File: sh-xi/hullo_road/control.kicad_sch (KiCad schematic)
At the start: 1 part, among them U1 ATtiny414-SS

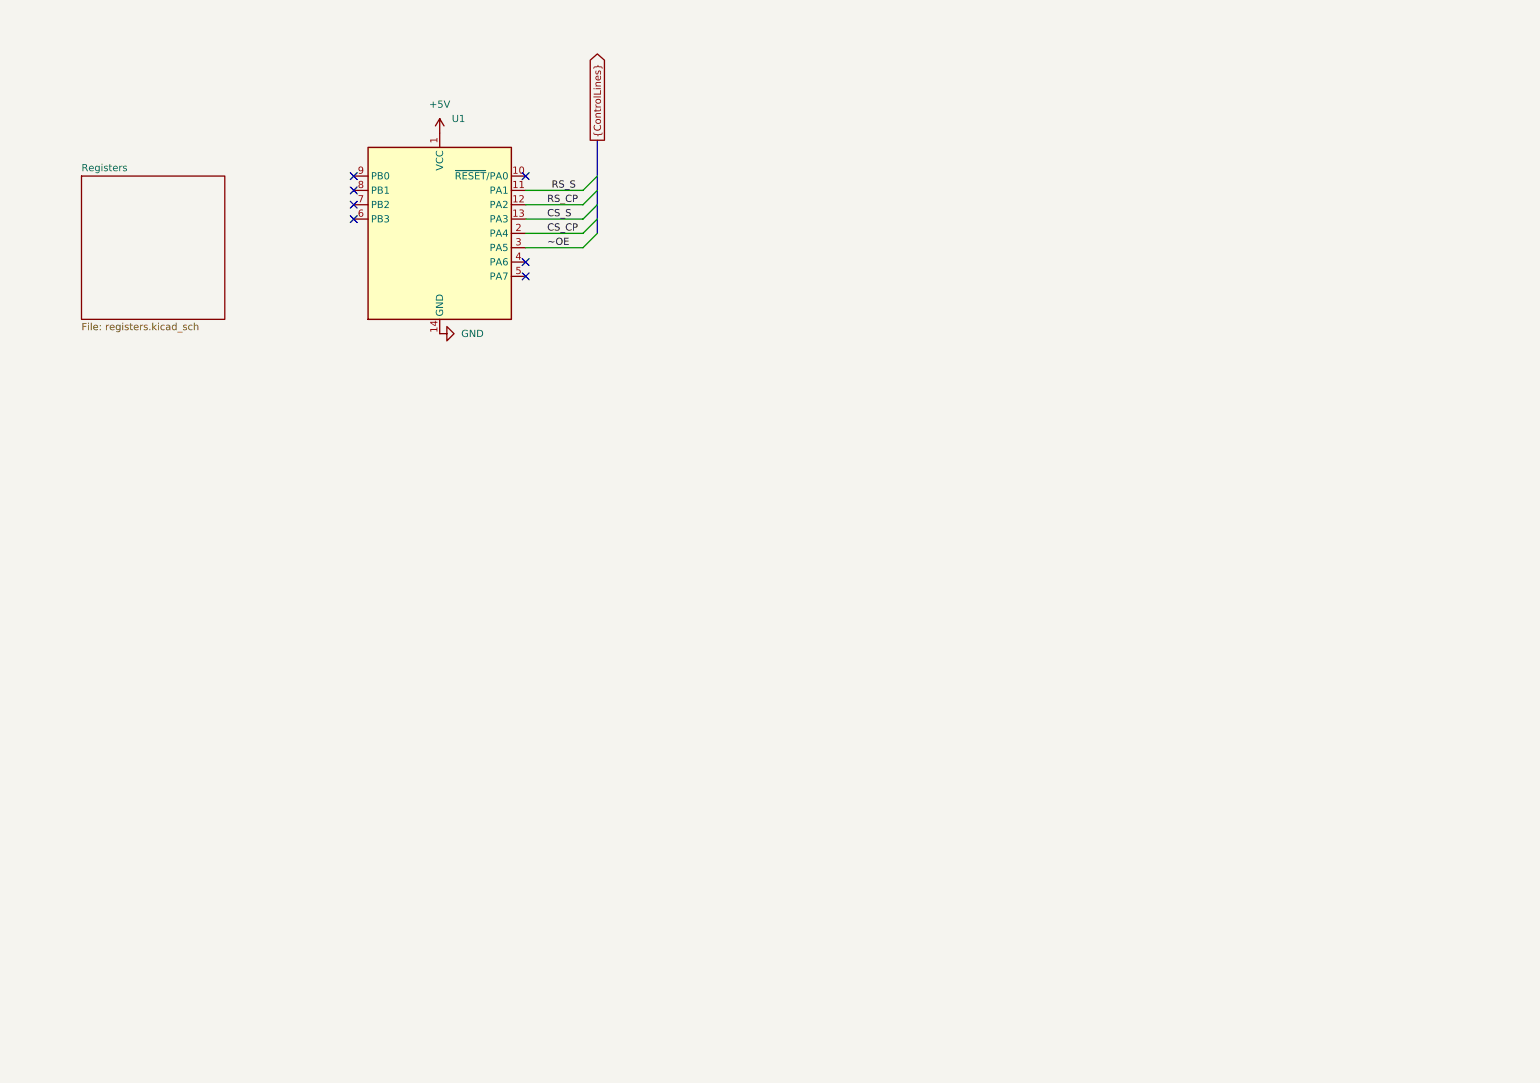
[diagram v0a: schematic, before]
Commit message: Create two board design and route most things
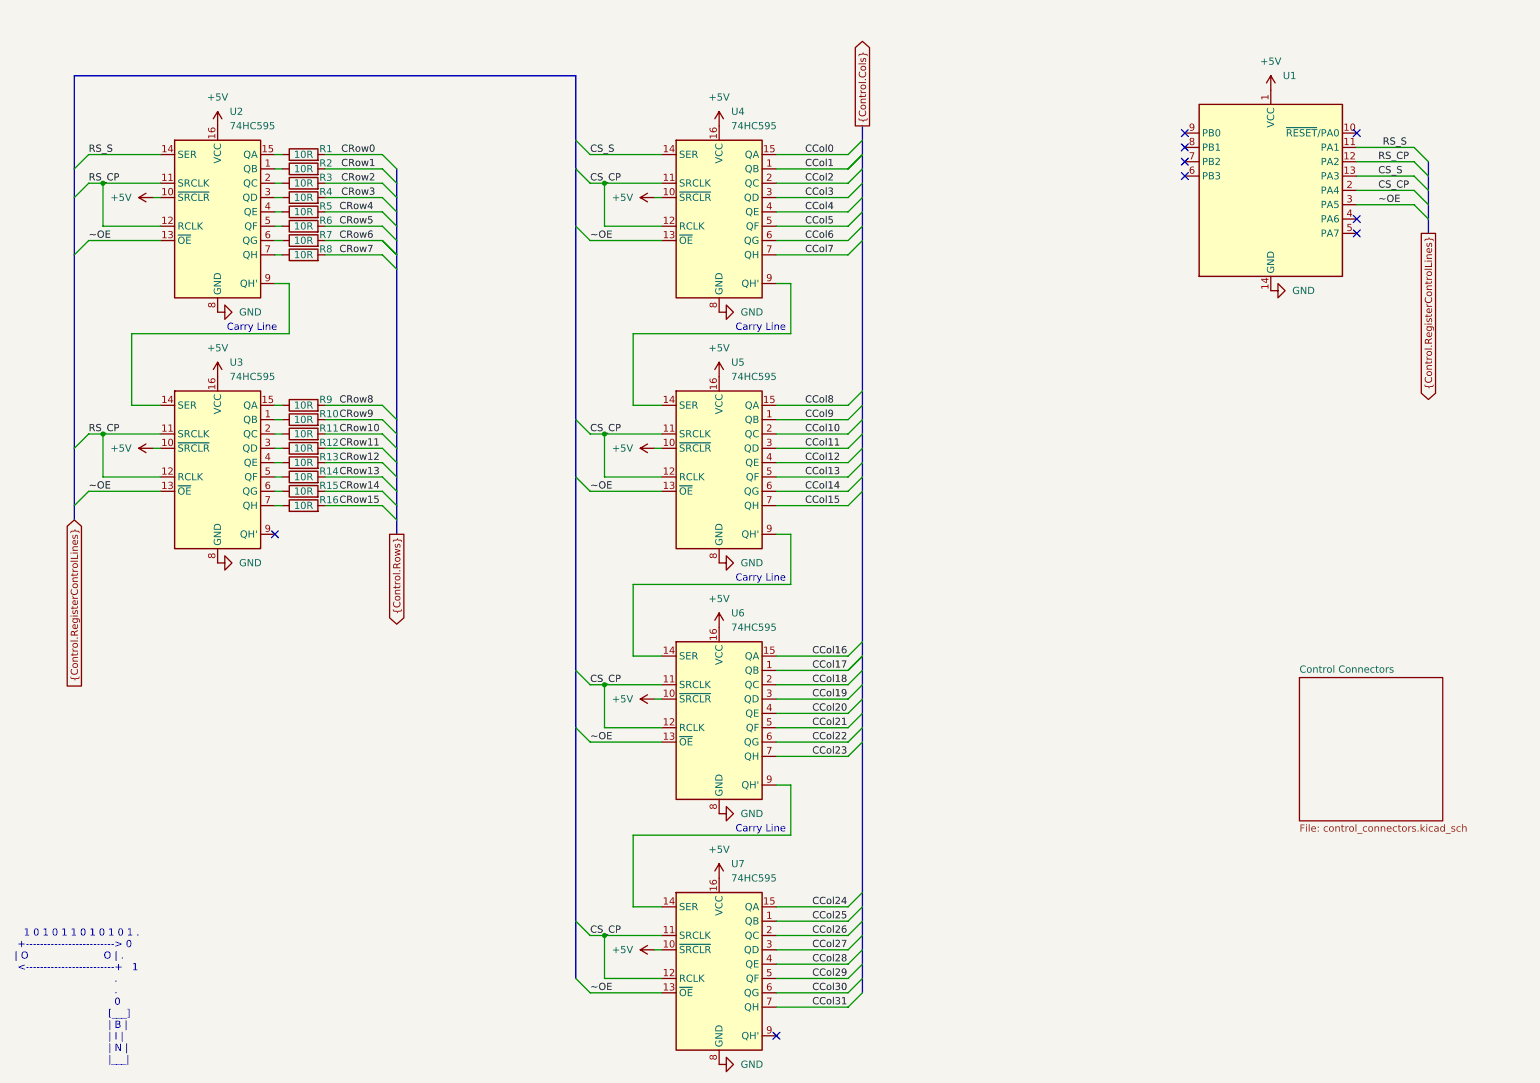
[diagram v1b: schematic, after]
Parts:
- added R1, R10, R11, R12, R13, R14, R15, R16, R2, R3, R4, R5, R6, R7, R8, R9: 10R, Resistor_SMD:R_0805_2012Metric, symbol Device:R
- added U2, U3, U4, U5, U6, U7: 74HC595, Package_SO:TSSOP-16_4.4x5mm_P0.65mm, symbol 74xx:74HC595
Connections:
- net +5V: now also U2.10 (~{SRCLR}), U2.16 (VCC), U3.10 (~{SRCLR}), U3.16 (VCC), U4.10 (~{SRCLR}), U4.16 (VCC), U5.10 (~{SRCLR}), U5.16 (VCC), U6.10 (~{SRCLR}), U6.16 (VCC), U7.10 (~{SRCLR}), U7.16 (VCC)
- net CS_CP: now also U4.11 (SRCLK), U4.12 (RCLK), U5.11 (SRCLK), U5.12 (RCLK), U6.11 (SRCLK), U6.12 (RCLK), U7.11 (SRCLK), U7.12 (RCLK)
- net CS_S: now also U4.14 (SER)
- net GND: now also U2.8 (GND), U3.8 (GND), U4.8 (GND), U5.8 (GND), U6.8 (GND), U7.8 (GND)
- net RS_CP: now also U2.11 (SRCLK), U2.12 (RCLK), U3.11 (SRCLK), U3.12 (RCLK)
- net RS_S: now also U2.14 (SER)
- net ~OE: now also U2.13 (~{OE}), U3.13 (~{OE}), U4.13 (~{OE}), U5.13 (~{OE}), U6.13 (~{OE}), U7.13 (~{OE})
- new net: R11.1, U3.2 (QC)
- new net: R13.1, U3.4 (QE)
- new net: R8.1, U2.7 (QH)
- new net: R4.1, U2.3 (QD)
- new net: R16.1, U3.7 (QH)
- new net: R12.1, U3.3 (QD)
- new net: R2.1, U2.1 (QB)
- new net: R3.1, U2.2 (QC)
- new net: R6.1, U2.5 (QF)
- new net: U6.9 (QH'), U7.14 (SER)
- new net: U5.9 (QH'), U6.14 (SER)
- new net: R9.1, U3.15 (QA)
- new net: R7.1, U2.6 (QG)
- new net: R5.1, U2.4 (QE)
- new net: R15.1, U3.6 (QG)
- new net: R14.1, U3.5 (QF)
- new net: R1.1, U2.15 (QA)
- new net: U4.9 (QH'), U5.14 (SER)
- new net: U2.9 (QH'), U3.14 (SER)
- new net: R10.1, U3.1 (QB)
- new net CCol0: U4.15 (QA)
- new net CCol1: U4.1 (QB)
- new net CCol10: U5.2 (QC)
- new net CCol11: U5.3 (QD)
- new net CCol12: U5.4 (QE)
- new net CCol13: U5.5 (QF)
- new net CCol14: U5.6 (QG)
- new net CCol15: U5.7 (QH)
- new net CCol16: U6.15 (QA)
- new net CCol17: U6.1 (QB)
- new net CCol18: U6.2 (QC)
- new net CCol19: U6.3 (QD)
- new net CCol2: U4.2 (QC)
- new net CCol20: U6.4 (QE)
- new net CCol21: U6.5 (QF)
- new net CCol22: U6.6 (QG)
- new net CCol23: U6.7 (QH)
- new net CCol24: U7.15 (QA)
- new net CCol25: U7.1 (QB)
- new net CCol26: U7.2 (QC)
- new net CCol27: U7.3 (QD)
- new net CCol28: U7.4 (QE)
- new net CCol29: U7.5 (QF)
- new net CCol3: U4.3 (QD)
- new net CCol30: U7.6 (QG)
- new net CCol31: U7.7 (QH)
- new net CCol4: U4.4 (QE)
- new net CCol5: U4.5 (QF)
- new net CCol6: U4.6 (QG)
- new net CCol7: U4.7 (QH)
- new net CCol8: U5.15 (QA)
- new net CCol9: U5.1 (QB)
- new net CRow0: R1.2
- new net CRow1: R2.2
- new net CRow10: R11.2
- new net CRow11: R12.2
- new net CRow12: R13.2
- new net CRow13: R14.2
- new net CRow14: R15.2
- new net CRow15: R16.2
- new net CRow2: R3.2
- new net CRow3: R4.2
- new net CRow4: R5.2
- new net CRow5: R6.2
- new net CRow6: R7.2
- new net CRow7: R8.2
- new net CRow8: R9.2
- new net CRow9: R10.2
- no-connect marks 7 -> 9
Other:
- removed sheet Registers
- added sheet Control Connectors (control_connectors.kicad_sch)
- note added: "1 0 1 0 1 1 0 1 0 1 0 1 . +-------------------------> 0 | O O | . <-------------------------+ 1 . . 0 [___] | B | | I | | N | |___|"
- note added: "Carry Line"
- moved on the sheet: U1
